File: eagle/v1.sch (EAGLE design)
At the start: 40 parts, among them IC2 LT1761, IC4 LT1376-ADJ, Q1 12Mhz, T1 Si2301DS, X1 USB-MICROB

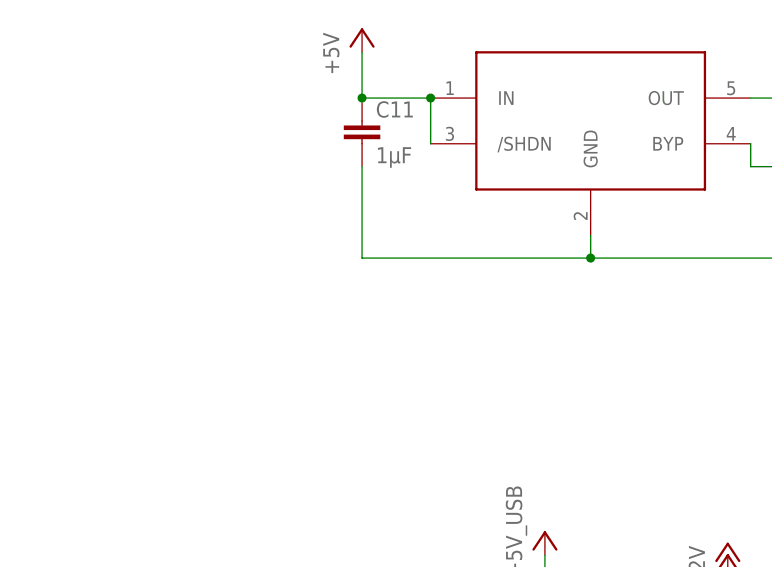
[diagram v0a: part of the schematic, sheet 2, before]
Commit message: two minor layout fixes
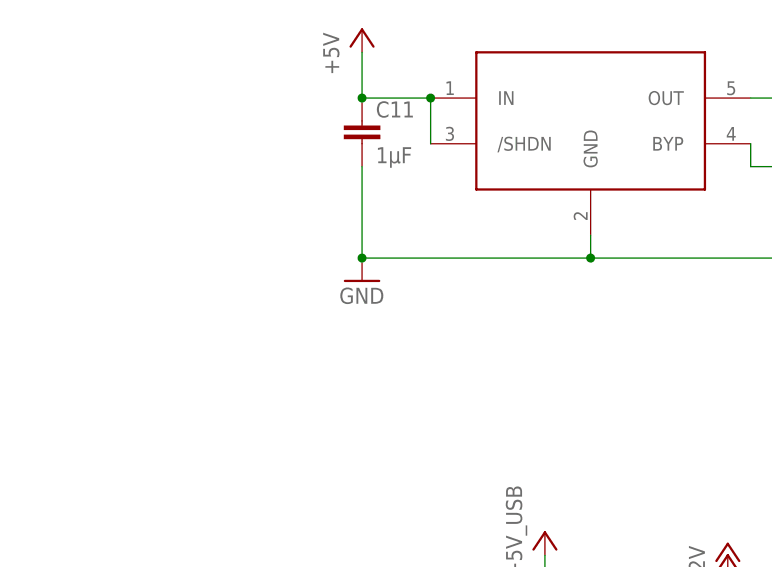
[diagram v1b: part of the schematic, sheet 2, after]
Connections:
- removed net N$9: C11.2, C12.-, IC2.GND
- net GND: now also C11.2, C12.-, IC2.GND
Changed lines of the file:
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@@
 <?xml version="1.0" encoding="utf-8"?>
 <!DOCTYPE eagle SYSTEM "eagle.dtd">
-<eagle version="6.3">
+<eagle version="6.4">
 <drawing>
 <settings>
@@
 <part name="P+5" library="supply1" deviceset="+12V" device=""/>
 <part name="P+6" library="supply1" deviceset="+12V" device=""/>
+<part name="GND7" library="supply1" deviceset="GND" device=""/>
 </parts>
 <sheets>
@@
 <instance part="GND6" gate="1" x="83.82" y="104.14"/>
 <instance part="P+6" gate="1" x="83.82" y="132.08"/>
+<instance part="GND7" gate="1" x="43.18" y="162.56"/>
 </instances>
 <busses>
@@
 <pinref part="GND6" gate="1" pin="GND"/>
 </segment>
+<segment>
+<pinref part="C11" gate="G$1" pin="2"/>
+<wire x1="43.18" y1="175.26" x2="43.18" y2="165.1" width="0.1524" layer="91"/>
+<pinref part="IC2" gate="G$1" pin="GND"/>
+<wire x1="43.18" y1="165.1" x2="68.58" y2="165.1" width="0.1524" layer="91"/>
+<wire x1="68.58" y1="165.1" x2="68.58" y2="167.64" width="0.1524" layer="91"/>
+<pinref part="C12" gate="G$1" pin="-"/>
+<wire x1="68.58" y1="165.1" x2="104.14" y2="165.1" width="0.1524" layer="91"/>
+<wire x1="104.14" y1="165.1" x2="104.14" y2="175.26" width="0.1524" layer="91"/>
+<junction x="68.58" y="165.1"/>
+<pinref part="GND7" gate="1" pin="GND"/>
+<junction x="43.18" y="165.1"/>
+</segment>
 </net>
 <net name="+3V3" class="0">
@@
 </segment>
 </net>
-<net name="N$9" class="0">
-<segment>
-<pinref part="C11" gate="G$1" pin="2"/>
-<wire x1="43.18" y1="175.26" x2="43.18" y2="165.1" width="0.1524" layer="91"/>
-<pinref part="IC2" gate="G$1" pin="GND"/>
-<wire x1="43.18" y1="165.1" x2="68.58" y2="165.1" width="0.1524" layer="91"/>
-<wire x1="68.58" y1="165.1" x2="68.58" y2="167.64" width="0.1524" layer="91"/>
-<pinref part="C12" gate="G$1" pin="-"/>
-<wire x1="68.58" y1="165.1" x2="104.14" y2="165.1" width="0.1524" layer="91"/>
-<wire x1="104.14" y1="165.1" x2="104.14" y2="175.26" width="0.1524" layer="91"/>
-<junction x="68.58" y="165.1"/>
-</segment>
-</net>
